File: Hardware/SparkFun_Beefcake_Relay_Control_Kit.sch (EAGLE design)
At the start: 17 parts, among them K1 JQX-15F, Q2 2N3904

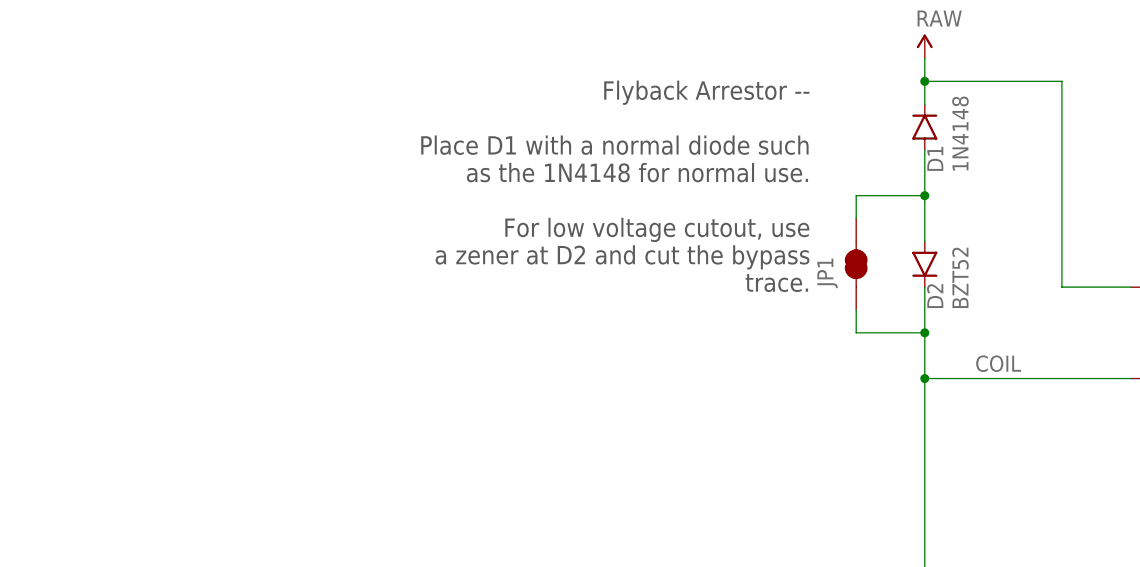
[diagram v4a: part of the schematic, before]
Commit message: updated silk for redboard review
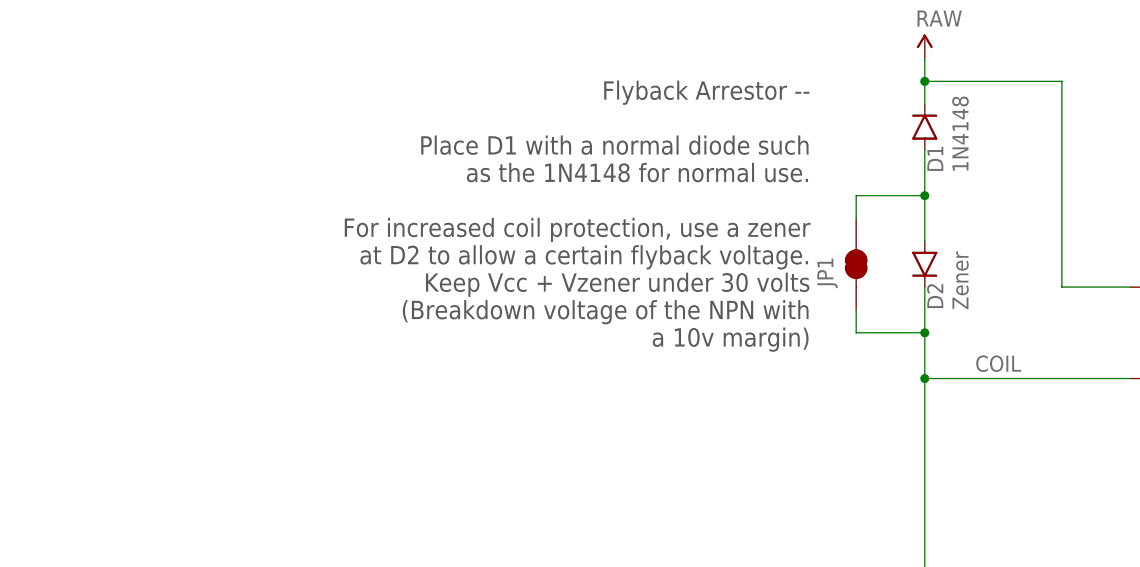
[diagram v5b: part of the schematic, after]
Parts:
- D2: value BZT52 -> Zener
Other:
- note added: "Flyback Arrestor -- Place D1 with a normal diode such as the 1N4148 for normal use. For increased coil protection, use a zener at D2 to allow a certain flyback voltage. Keep Vcc + Vzener under 30 volts (Breakdown voltage of the NPN with a 10v margin)"
- note removed: "Flyback Arrestor -- Place D1 with a normal diode such as the 1N4148 for normal use. For low voltage cutout, use a zener at D2 and cut the bypass trace."
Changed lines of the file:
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@@
 <attribute name="PROD_ID" value="CONN-10134"/>
 </part>
-<part name="D2" library="SparkFun-DiscreteSemi" deviceset="DIODE" device="KIT" value="BZT52">
+<part name="D2" library="SparkFun-DiscreteSemi" deviceset="DIODE" device="KIT" value="Zener">
 <attribute name="PROD-ID" value="DIO-08199"/>
 </part>
@@
 Place D1 with a normal diode such
 as the 1N4148 for normal use.
-For low voltage cutout, use
-a zener at D2 and cut the bypass
-trace.</text>
+For increased coil protection, use a zener
+at D2 to allow a certain flyback voltage.
+Keep Vcc + Vzener under 30 volts
+(Breakdown voltage of the NPN with
+a 10v margin)</text>
 <text x="10.16" y="22.86" size="2.032" layer="97">To maintiain 250VAC/VDC galvanic isolation, use
 non-conductive standoffs and 4-40 HW with a head

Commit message: Finished for reds review, implemented changes
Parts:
- D2: device SparkFun-DiscreteSemi:DIODEKIT -> SparkFun-DiscreteSemi:DIODE-ZENER; PROD-ID DIO-08199 -> (none)
- JP1: value JUMPER-PAD-2-NC_BY_TRACE -> JUMPER-PAD-2-NOYES_SILK; device SparkFun-Passives:JUMPER-PAD-2-NC_BY_TRACE -> SparkFun-Passives:JUMPER-PAD-2-NOYES_SILK
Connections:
- net RAW renamed VCC
- new net DIODENODE: D1.A, D2.A, JP1.2
- net COIL: no longer D1.A, D2.A, JP1.2
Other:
- note added: "Flyback Arrestor -- Place D1 with a normal diode such as the 1N4148 for all cases. For increased coil protection, use a zener at D2 to allow a certain flyback voltage. Keep Vcc + Vzener under 30 volts (Breakdown voltage of the NPN with a 10v margin) The zener is not critical for protection of the circuit, but helps allow the contacts to open faster. It can be bypassed by shorting JP1."
- note added: "Sparkfun Beefcake Relay Control"
- note added: "VCC CTRL GND"
- note added: "VCC requirements: 4-6V 150mA CTRL requirements: Relay on above 2.6V Relay off below 0.9V 5mA"
- note removed: "Flyback Arrestor -- Place D1 with a normal diode such as the 1N4148 for normal use. For increased coil protection, use a zener at D2 to allow a certain flyback voltage. Keep Vcc + Vzener under 30 volts (Breakdown voltage of the NPN with a 10v margin)"
- note removed: "Supply RAW with 5v DC"
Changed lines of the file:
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@@
 <part name="Q2" library="SparkFun-DiscreteSemi" deviceset="TRANSISTOR_NPN" device="2N3904-EZ" value="2N3904"/>
 <part name="GND1" library="SparkFun" deviceset="GND" device=""/>
-<part name="U$2" library="SparkFun" deviceset="RAW" device=""/>
+<part name="VCC" library="SparkFun-Aesthetics" deviceset="VCC" device=""/>
 <part name="R2" library="SparkFun-Resistors" deviceset="1KOHM-1/4W-1%(PTH)" device="HORIZ-KIT" value="1K"/>
 <part name="LED1" library="SparkFun-LED" deviceset="LED" device="5MM-KIT">
@@
 <attribute name="PROD_ID" value="DIO-08378"/>
 </part>
-<part name="U$10" library="SparkFun" deviceset="RAW" device=""/>
+<part name="U$10" library="SparkFun-Aesthetics" deviceset="VCC" device=""/>
 <part name="GND2" library="SparkFun" deviceset="GND" device=""/>
 <part name="J2" library="SparkFun-Connectors" deviceset="M03" device="SCREW"/>
-<part name="U$8" library="SparkFun" deviceset="RAW" device=""/>
+<part name="U$8" library="SparkFun-Aesthetics" deviceset="VCC" device=""/>
 <part name="K1" library="SparkFun-Electromechanical" deviceset="RELAY" device="PTH5" value="JQX-15F"/>
 <part name="U$12" library="SparkFun" deviceset="OSHW-LOGO" device="S"/>
@@
 <attribute name="PROD_ID" value="CONN-10134"/>
 </part>
-<part name="D2" library="SparkFun-DiscreteSemi" deviceset="DIODE" device="KIT" value="Zener">
-<attribute name="PROD-ID" value="DIO-08199"/>
-</part>
 <part name="FRAME2" library="SparkFun-Aesthetics" deviceset="FRAME-LETTER" device=""/>
 <part name="LOGO1" library="SparkFun-Aesthetics" deviceset="SFE_LOGO_NAME_FLAME" device=".1_INCH" value="SFE_LOGO_NAME_FLAME.1_INCH"/>
-<part name="JP1" library="SparkFun-Passives" deviceset="JUMPER-PAD-2-NC_BY_TRACE" device=""/>
+<part name="JP1" library="SparkFun-Passives" deviceset="JUMPER-PAD-2-NO" device="YES_SILK"/>
+<part name="D2" library="SparkFun-DiscreteSemi" deviceset="DIODE-ZENER" device="" value="Zener"/>
 </parts>
 <sheets>
@@
 <text x="142.24" y="86.36" size="2.032" layer="97">Relay drive indicator -- Illuminates
 when the relay coil is energized</text>
-<text x="93.98" y="152.4" size="2.032" layer="97" rot="R180">Flyback Arrestor --
+<text x="10.16" y="149.86" size="2.032" layer="97" align="top-left">Flyback Arrestor --
 Place D1 with a normal diode such
-as the 1N4148 for normal use.
+as the 1N4148 for all cases.
 For increased coil protection, use a zener
 at D2 to allow a certain flyback voltage.
 Keep Vcc + Vzener under 30 volts
 (Breakdown voltage of the NPN with
-a 10v margin)</text>
+a 10v margin)
+The zener is not critical for protection of
+the circuit, but helps allow the contacts to
+open faster.  It can be bypassed by shorting JP1.</text>
 <text x="10.16" y="22.86" size="2.032" layer="97">To maintiain 250VAC/VDC galvanic isolation, use
 non-conductive standoffs and 4-40 HW with a head
@@
 conductive chassis, standoff diameter must be less
 than 0.21 inch.</text>
-<text x="63.5" y="68.58" size="2.032" layer="97">Supply RAW with 5v DC</text>
+<text x="10.16" y="73.66" size="2.032" layer="97" align="top-left">VCC requirements:
+  4-6V
+  150mA
+CTRL requirements:
+  Relay on above 2.6V
+  Relay off below 0.9V
+  5mA</text>
+<text x="62.738" y="53.34" size="2.032" layer="97" align="center-right">VCC
+CTRL
+GND</text>
+<text x="10.16" y="172.72" size="4.064" layer="97">Sparkfun Beefcake Relay Control</text>
 </plain>
 <instances>
 <instance part="Q2" gate="G$1" x="104.14" y="53.34"/>
 <instance part="GND1" gate="1" x="106.68" y="43.18"/>
-<instance part="U$2" gate="G$1" x="106.68" y="154.94"/>
+<instance part="VCC" gate="G$1" x="106.68" y="154.94"/>
 <instance part="R2" gate="G$1" x="91.44" y="53.34" rot="R180"/>
 <instance part="LED1" gate="G$1" x="134.62" y="88.9" smashed="yes">
@@
 <attribute name="PROD_ID" x="182.88" y="139.7" size="1.27" layer="96" rot="R180" display="off"/>
 </instance>
-<instance part="D2" gate="G$1" x="106.68" y="132.08" smashed="yes" rot="R270">
-<attribute name="NAME" x="108.7374" y="127" size="1.778" layer="95" rot="R90"/>
-<attribute name="VALUE" x="111.5314" y="127" size="1.778" layer="96" rot="R90"/>
-</instance>
 <instance part="FRAME2" gate="G$1" x="0" y="0"/>
 <instance part="FRAME2" gate="V" x="147.32" y="0"/>
@@
 <attribute name="NAME" x="96.52" y="129.54" size="1.778" layer="95" rot="R90"/>
 </instance>
+<instance part="D2" gate="G$1" x="106.68" y="132.08" smashed="yes" rot="R270">
+<attribute name="NAME" x="108.7374" y="127" size="1.778" layer="95" rot="R90"/>
+<attribute name="VALUE" x="111.5314" y="127" size="1.778" layer="96" rot="R90"/>
+</instance>
 </instances>
 <busses>
@@
 </segment>
 </net>
-<net name="RAW" class="0">
+<net name="VCC" class="0">
 <segment>
 <wire x1="106.68" y1="149.86" x2="106.68" y2="152.4" width="0.1524" layer="91"/>
@@
 <wire x1="106.68" y1="152.4" x2="106.68" y2="154.94" width="0.1524" layer="91"/>
 <junction x="106.68" y="152.4"/>
-<pinref part="U$2" gate="G$1" pin="RAW"/>
+<pinref part="VCC" gate="G$1" pin="VCC"/>
 <pinref part="D1" gate="G$1" pin="C"/>
 <pinref part="K1" gate="K$1" pin="COIL1"/>
@@
 <wire x1="134.62" y1="93.98" x2="134.62" y2="91.44" width="0.1524" layer="91"/>
 <pinref part="LED1" gate="G$1" pin="A"/>
-<pinref part="U$10" gate="G$1" pin="RAW"/>
+<pinref part="U$10" gate="G$1" pin="VCC"/>
 </segment>
 <segment>
@@
 <wire x1="81.28" y1="55.88" x2="81.28" y2="58.42" width="0.1524" layer="91"/>
 <pinref part="J2" gate="G$1" pin="3"/>
-<pinref part="U$8" gate="G$1" pin="RAW"/>
+<pinref part="U$8" gate="G$1" pin="VCC"/>
 </segment>
 </net>
@@
 <pinref part="K1" gate="K$1" pin="COIL2"/>
 <wire x1="106.68" y1="119.38" x2="129.54" y2="119.38" width="0.1524" layer="91"/>
-<pinref part="D2" gate="G$1" pin="C"/>
-<wire x1="106.68" y1="129.54" x2="106.68" y2="124.46" width="0.1524" layer="91"/>
+<wire x1="106.68" y1="127" x2="106.68" y2="124.46" width="0.1524" layer="91"/>
 <wire x1="106.68" y1="119.38" x2="106.68" y2="124.46" width="0.1524" layer="91"/>
 <wire x1="106.68" y1="124.46" x2="99.06" y2="124.46" width="0.1524" layer="91"/>
@@
 <junction x="106.68" y="119.38"/>
 <junction x="106.68" y="68.58"/>
+<pinref part="D2" gate="G$1" pin="C"/>
+<wire x1="106.68" y1="129.54" x2="106.68" y2="127" width="0.1524" layer="91"/>
 <pinref part="JP1" gate="G$1" pin="1"/>
-<wire x1="99.06" y1="127" x2="99.06" y2="124.46" width="0.2032" layer="91"/>
-</segment>
-<segment>
-<pinref part="JP1" gate="G$1" pin="2"/>
-<pinref part="D1" gate="G$1" pin="A"/>
-<wire x1="106.68" y1="144.78" x2="106.68" y2="139.7" width="0.1524" layer="91"/>
-<pinref part="D2" gate="G$1" pin="A"/>
-<wire x1="106.68" y1="134.62" x2="106.68" y2="139.7" width="0.1524" layer="91"/>
-<junction x="106.68" y="139.7"/>
-<wire x1="106.68" y1="139.7" x2="99.06" y2="139.7" width="0.1524" layer="91"/>
-<wire x1="99.06" y1="139.7" x2="99.06" y2="137.16" width="0.2032" layer="91"/>
+<wire x1="99.06" y1="127" x2="99.06" y2="124.46" width="0.1524" layer="91"/>
 </segment>
 </net>
@@
 </segment>
 </net>
+<net name="DIODENODE" class="0">
+<segment>
+<pinref part="D1" gate="G$1" pin="A"/>
+<wire x1="106.68" y1="144.78" x2="106.68" y2="139.7" width="0.1524" layer="91"/>
+<junction x="106.68" y="139.7"/>
+<wire x1="106.68" y1="137.16" x2="106.68" y2="139.7" width="0.1524" layer="91"/>
+<wire x1="106.68" y1="139.7" x2="99.06" y2="139.7" width="0.1524" layer="91"/>
+<pinref part="D2" gate="G$1" pin="A"/>
+<wire x1="106.68" y1="137.16" x2="106.68" y2="134.62" width="0.1524" layer="91"/>
+<pinref part="JP1" gate="G$1" pin="2"/>
+<wire x1="99.06" y1="137.16" x2="99.06" y2="139.7" width="0.1524" layer="91"/>
+</segment>
+</net>

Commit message: Resolved github issues
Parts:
- renumbered Q2 to Q1, R4 to R3
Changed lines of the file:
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@@
 </classes>
 <parts>
-<part name="Q2" library="SparkFun-DiscreteSemi" deviceset="TRANSISTOR_NPN" device="2N3904-EZ" value="2N3904"/>
+<part name="Q1" library="SparkFun-DiscreteSemi" deviceset="TRANSISTOR_NPN" device="2N3904-EZ" value="2N3904"/>
 <part name="GND1" library="SparkFun" deviceset="GND" device=""/>
 <part name="VCC" library="SparkFun-Aesthetics" deviceset="VCC" device=""/>
@@
 <attribute name="PROD_ID" value="DIO-09529"/>
 </part>
-<part name="R4" library="SparkFun-Resistors" deviceset="1KOHM-1/4W-1%(PTH)" device="HORIZ-KIT" value="1K"/>
+<part name="R3" library="SparkFun-Resistors" deviceset="1KOHM-1/4W-1%(PTH)" device="HORIZ-KIT" value="1K"/>
 <part name="U$3" library="SparkFun" deviceset="STAND-OFF" device=""/>
 <part name="U$4" library="SparkFun" deviceset="STAND-OFF" device=""/>
@@
 </plain>
 <instances>
-<instance part="Q2" gate="G$1" x="104.14" y="53.34"/>
+<instance part="Q1" gate="G$1" x="104.14" y="53.34"/>
 <instance part="GND1" gate="1" x="106.68" y="43.18"/>
 <instance part="VCC" gate="G$1" x="106.68" y="154.94"/>
@@
 <attribute name="VALUE" x="140.335" y="84.328" size="1.778" layer="96" rot="R90"/>
 </instance>
-<instance part="R4" gate="G$1" x="134.62" y="76.2" rot="R90"/>
+<instance part="R3" gate="G$1" x="134.62" y="76.2" rot="R90"/>
 <instance part="U$3" gate="G$1" x="246.38" y="25.4"/>
 <instance part="U$4" gate="G$1" x="241.3" y="25.4"/>
@@
 <segment>
 <wire x1="106.68" y1="45.72" x2="106.68" y2="48.26" width="0.1524" layer="91"/>
-<pinref part="Q2" gate="G$1" pin="E"/>
+<pinref part="Q1" gate="G$1" pin="E"/>
 <pinref part="GND1" gate="1" pin="GND"/>
 </segment>
@@
 <segment>
 <wire x1="96.52" y1="53.34" x2="101.6" y2="53.34" width="0.1524" layer="91"/>
-<pinref part="Q2" gate="G$1" pin="B"/>
+<pinref part="Q1" gate="G$1" pin="B"/>
 <pinref part="R2" gate="G$1" pin="1"/>
 </segment>
@@
 <wire x1="134.62" y1="81.28" x2="134.62" y2="83.82" width="0.1524" layer="91"/>
 <pinref part="LED1" gate="G$1" pin="C"/>
-<pinref part="R4" gate="G$1" pin="2"/>
+<pinref part="R3" gate="G$1" pin="2"/>
 </segment>
 </net>
@@
 <wire x1="134.62" y1="68.58" x2="134.62" y2="71.12" width="0.1524" layer="91"/>
 <label x="112.268" y="120.142" size="1.778" layer="95"/>
-<pinref part="Q2" gate="G$1" pin="C"/>
-<pinref part="R4" gate="G$1" pin="1"/>
+<pinref part="Q1" gate="G$1" pin="C"/>
+<pinref part="R3" gate="G$1" pin="1"/>
 <wire x1="106.68" y1="58.42" x2="106.68" y2="68.58" width="0.1524" layer="91"/>
 <wire x1="106.68" y1="68.58" x2="106.68" y2="119.38" width="0.1524" layer="91"/>
